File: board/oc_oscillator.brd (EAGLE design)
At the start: 40 x 23 mm, 13 parts, among them T1 BC547, X1 BU-SMA-V, X2 C-GRID-02-70543

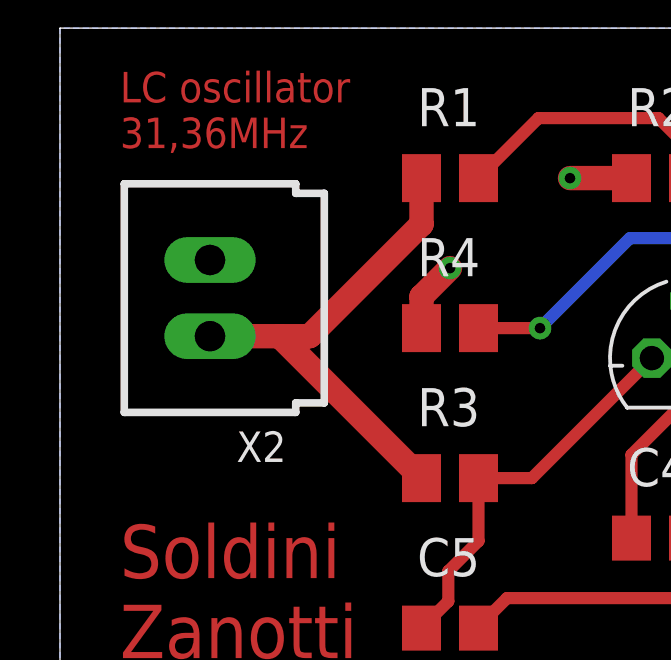
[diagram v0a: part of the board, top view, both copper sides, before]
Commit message: ✏️ Add 9v label to board
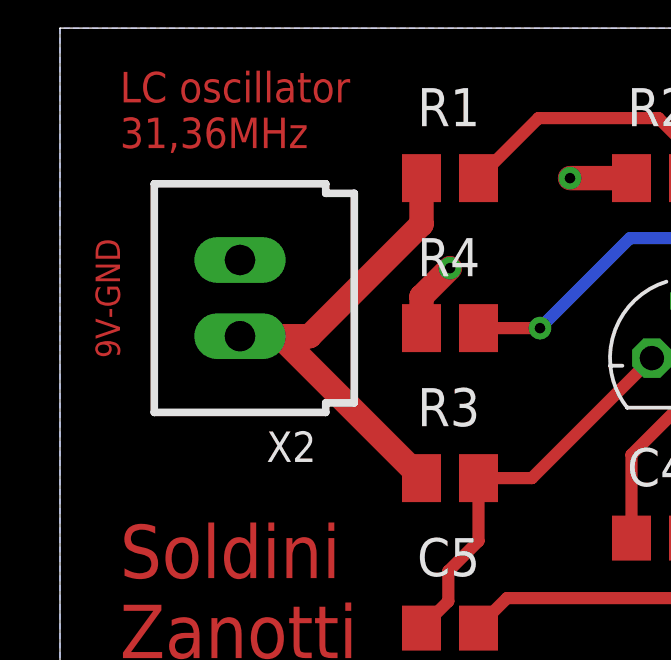
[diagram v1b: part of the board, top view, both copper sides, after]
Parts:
- moved X2 1.00 mm to (10.0, 18.0)
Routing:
- net VCC: track 16.9 -> 15.9 mm
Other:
- board text added: "9V-GND"
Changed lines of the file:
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@@
 </layers>
 <board>
-<fusionsync huburn="a.cGVyc29uYWw6dWUyZDk3ZjVk" projecturn="a.cGVyc29uYWw6dWUyZDk3ZjVkIzIwMjAxMjE3MzYzNDQ2NTc2" f3durn="urn:adsk.wipprod:dm.lineage:0bACjzofTNSSE8O8HOe8bA" pcbguid="" lastpulledtime="" lastsyncedchangeguid="" latestrevisionid="c96f1192-dd9f-47ad-8095-a9292b0931be" lastsyncedrevisionid="c96f1192-dd9f-47ad-8095-a9292b0931be" lastboardhashguid="3d7e4a74-b200-879d-c51e-ee22851088ce" lastpushedtime="2023-06-12T17:22:39Z" linktopcb3d="true"/>
+<fusionsync huburn="a.cGVyc29uYWw6dWUyZDk3ZjVk" projecturn="a.cGVyc29uYWw6dWUyZDk3ZjVkIzIwMjAxMjE3MzYzNDQ2NTc2" f3durn="urn:adsk.wipprod:dm.lineage:0bACjzofTNSSE8O8HOe8bA" pcbguid="" lastpulledtime="" lastsyncedchangeguid="" latestrevisionid="c96f1192-dd9f-47ad-8095-a9292b0931be" lastsyncedrevisionid="c96f1192-dd9f-47ad-8095-a9292b0931be" lastboardhashguid="3d7e4a74-b200-879d-c51e-ee22851088ce" lastpushedtime="2023-06-12T17:22:39Z" linktopcb3d="false"/>
 <plain>
 <wire x1="4" y1="4" x2="44" y2="4" width="0" layer="20"/>
@@
 <text x="6" y="23" size="1.016" layer="1">LC oscillator
 31,36MHz</text>
+<text x="6" y="16" size="0.8128" layer="1" rot="R90">9V-GND</text>
 </plain>
 <attributes>
@@
 <attribute name="POPULARITY" value="6" x="57.05" y="3.65" size="1.778" layer="27" display="off"/>
 </element>
-<element name="X2" library="con-molex" library_urn="urn:adsk.eagle:library:165" package="70543-02" package3d_urn="urn:adsk.eagle:package:8078681/1" value="C-GRID-02-70543" x="9" y="18" smashed="yes" rot="R90">
-<attribute name="MF" value="MOLEX" x="14.08" y="48.48" size="1.778" layer="27" rot="R90" display="off"/>
-<attribute name="MPN" value="" x="14.08" y="48.48" size="1.778" layer="27" rot="R90" display="off"/>
-<attribute name="NAME" x="11.54" y="13.555" size="1.016" layer="25" ratio="10" rot="R180"/>
-<attribute name="OC_FARNELL" value="unknown" x="14.08" y="48.48" size="1.778" layer="27" rot="R90" display="off"/>
-<attribute name="OC_NEWARK" value="unknown" x="14.08" y="48.48" size="1.778" layer="27" rot="R90" display="off"/>
-<attribute name="POPULARITY" value="1" x="14.08" y="48.48" size="1.778" layer="27" rot="R90" display="off"/>
+<element name="X2" library="con-molex" library_urn="urn:adsk.eagle:library:165" package="70543-02" package3d_urn="urn:adsk.eagle:package:8078681/1" value="C-GRID-02-70543" x="10" y="18" smashed="yes" rot="R90">
+<attribute name="MF" value="MOLEX" x="15.08" y="48.48" size="1.778" layer="27" rot="R90" display="off"/>
+<attribute name="MPN" value="" x="15.08" y="48.48" size="1.778" layer="27" rot="R90" display="off"/>
+<attribute name="NAME" x="12.54" y="13.555" size="1.016" layer="25" ratio="10" rot="R180"/>
+<attribute name="OC_FARNELL" value="unknown" x="15.08" y="48.48" size="1.778" layer="27" rot="R90" display="off"/>
+<attribute name="OC_NEWARK" value="unknown" x="15.08" y="48.48" size="1.778" layer="27" rot="R90" display="off"/>
+<attribute name="POPULARITY" value="1" x="15.08" y="48.48" size="1.778" layer="27" rot="R90" display="off"/>
 </element>
 </elements>
@@
 <contactref element="R3" pad="1"/>
 <wire x1="16" y1="22" x2="16.05" y2="22" width="0.8128" layer="1"/>
-<wire x1="9" y1="16.73" x2="11.32" y2="16.73" width="0.8128" layer="1"/>
+<wire x1="10" y1="16.73" x2="11.32" y2="16.73" width="0.8128" layer="1"/>
 <wire x1="11.32" y1="16.73" x2="12.32" y2="16.73" width="0.8128" layer="1"/>
 <wire x1="11.32" y1="16.73" x2="16.05" y2="12" width="0.8128" layer="1"/>
